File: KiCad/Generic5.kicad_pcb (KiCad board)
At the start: 2 copper layers, 12.5 x 31 mm, 28 parts, among them J1 Conn_01x04, J2 USB-C, U1 ESP32-PICO-MINI-02, U2 FT231XQ, U3 LMR16006+FB

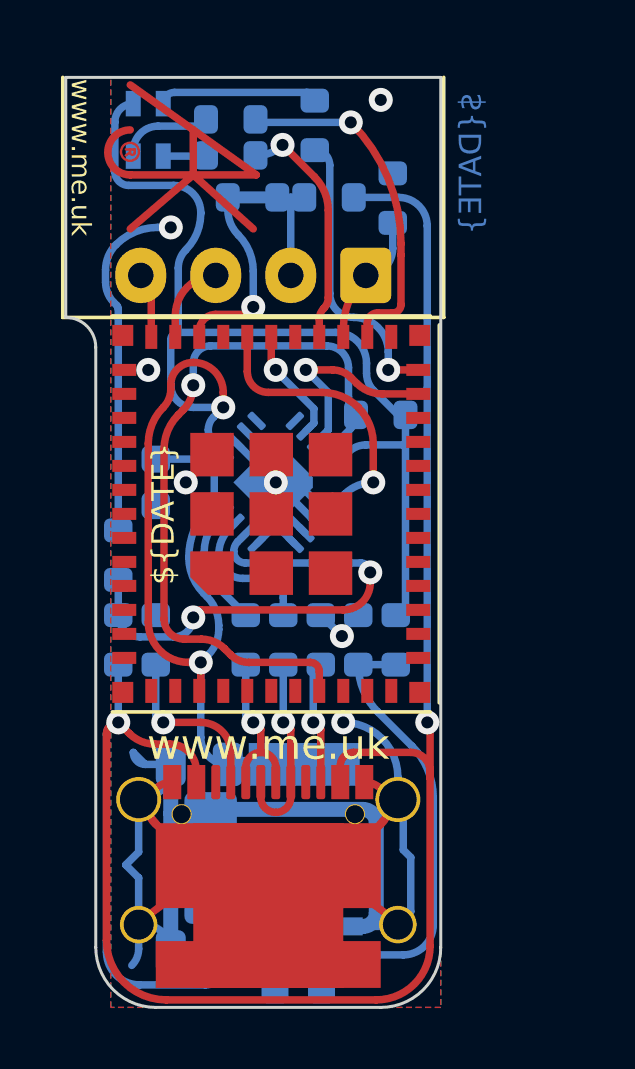
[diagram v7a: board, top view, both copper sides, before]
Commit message: Added buzzer
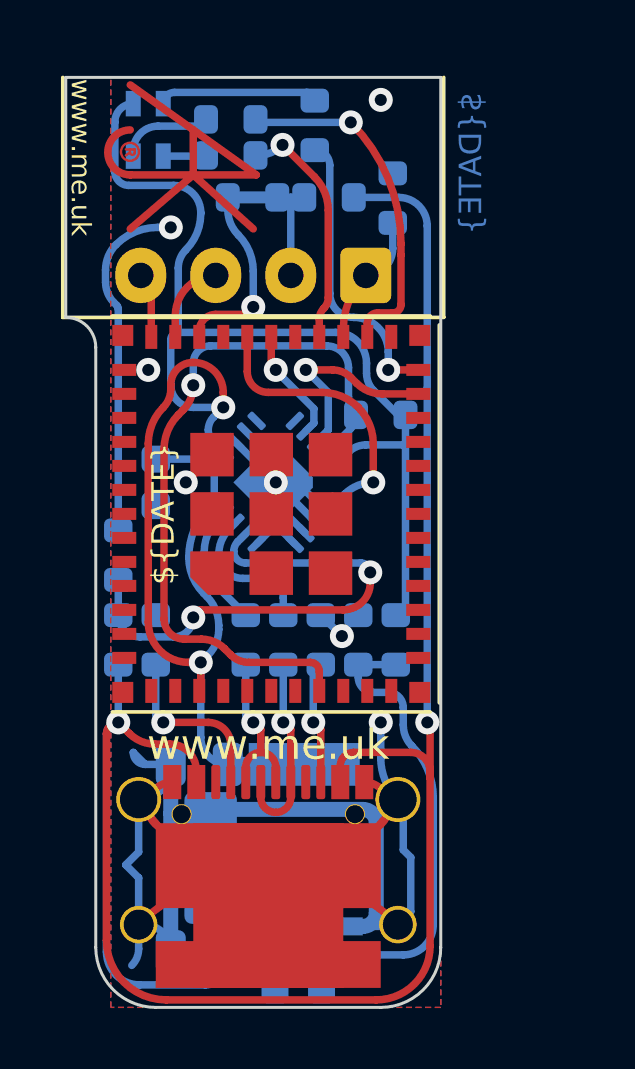
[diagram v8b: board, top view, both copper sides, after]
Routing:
- net GND: track 46.6 -> 45.7 mm
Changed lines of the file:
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@@
   (segment (start 152.375 33.625) (end 151.5 34.5) (width 0.25) (layer "F.Cu") (net 1))
   (via (at 150.25 30.75) (size 0.8) (drill 0.4) (layers "F.Cu" "B.Cu") (free) (net 1))
-  (via (at 156.75 42.5) (size 0.8) (drill 0.4) (layers "F.Cu" "B.Cu") (free) (net 1))
+  (via (at 158 42.5) (size 0.8) (drill 0.4) (layers "F.Cu" "B.Cu") (free) (net 1))
   (via (at 154.5 34.5) (size 0.8) (drill 0.4) (layers "F.Cu" "B.Cu") (net 1))
   (via (at 151 26) (size 0.8) (drill 0.4) (layers "F.Cu" "B.Cu") (free) (net 1))
@@
   (segment (start 158.51 49.3) (end 156.85 49.3) (width 0.25) (layer "B.Cu") (net 1))
   (segment (start 149.93 47.68) (end 149.5 47.25) (width 0.25) (layer "B.Cu") (net 1))
-  (segment (start 158.57 44.32) (end 158.57 45.07) (width 0.25) (layer "B.Cu") (net 1))
   (segment (start 159 47) (end 159 48.81) (width 0.25) (layer "B.Cu") (net 1))
   (segment (start 158.57 45.07) (end 158.75 45.25) (width 0.25) (layer "B.Cu") (net 1))
@@
   (segment (start 158.75 45.25) (end 158.75 46.75) (width 0.25) (layer "B.Cu") (net 1))
   (segment (start 149.5 47.25) (end 149.93 46.82) (width 0.25) (layer "B.Cu") (net 1))
+  (segment (start 158 42.5) (end 158 43.693899) (width 0.25) (layer "B.Cu") (net 1))
   (segment (start 154.375 34.375) (end 154.5 34.5) (width 0.25) (layer "B.Cu") (net 1))
   (segment (start 149.108578 28.508578) (end 149.2 28.6) (width 0.25) (layer "B.Cu") (net 1))
@@
   (arc (start 150.09 49.24) (mid 150.733467 49.506533) (end 151 50.15) (width 0.25) (layer "B.Cu") (net 1))
   (arc (start 151 44) (mid 150.686604 44.756604) (end 149.93 45.07) (width 0.25) (layer "B.Cu") (net 1))
-  (arc (start 156.75 42.5) (mid 158.036934 43.033066) (end 158.57 44.32) (width 0.25) (layer "B.Cu") (net 1))
   (arc (start 149.175 26.575) (mid 148.916317 26.962145) (end 148.82548 27.418815) (width 0.25) (layer "B.Cu") (net 1))
   (arc (start 148.82548 27.825119) (mid 148.899055 28.195004) (end 149.108578 28.508578) (width 0.25) (layer "B.Cu") (net 1))
@@
   (arc (start 149.93 50.044731) (mid 149.870225 50.34524) (end 149.7 50.6) (width 0.25) (layer "B.Cu") (net 1))
   (arc (start 149.175 26.575) (mid 149.811898 26.149438) (end 150.563172 26) (width 0.25) (layer "B.Cu") (net 1))
+  (arc (start 158 43.693899) (mid 158.148138 44.438639) (end 158.57 45.07) (width 0.25) (layer "B.Cu") (net 1))
   (arc (start 158.57 49.24) (mid 158.552426 49.282426) (end 158.51 49.3) (width 0.25) (layer "B.Cu") (net 1))
   (segment (start 156.65 44.49) (end 156.65 43.95) (width 0.25) (layer "F.Cu") (net 2))
@@
   (segment (start 156.788909 34.898097) (end 156.55061 35.136396) (width 0.25) (layer "B.Cu") (net 28))
   (arc (start 157.75 34.5) (mid 157.229861 34.603462) (end 156.788909 34.898097) (width 0.25) (layer "B.Cu") (net 28))
-  (segment (start 157.904074 42.154074) (end 159.042893 43.292893) (width 0.25) (layer "B.Cu") (net 30))
+  (segment (start 157.75 41.5) (end 158.25 41.5) (width 0.25) (layer "B.Cu") (net 30))
+  (segment (start 158.75 42) (end 158.75 42.585787) (width 0.25) (layer "B.Cu") (net 30))
+  (segment (start 157.25 40.575) (end 157.25 41) (width 0.25) (layer "B.Cu") (net 30))
   (segment (start 157.25 40.575) (end 158.5 40.575) (width 0.25) (layer "B.Cu") (net 30))
   (segment (start 158.75 50.25) (end 156.85 50.25) (width 0.25) (layer "B.Cu") (net 30))
   (segment (start 159.75 45) (end 159.75 49.25) (width 0.25) (layer "B.Cu") (net 30))
-  (arc (start 157.25 40.575) (mid 157.419988 41.429589) (end 157.904074 42.154074) (width 0.25) (layer "B.Cu") (net 30))
   (arc (start 159.75 49.25) (mid 159.457107 49.957107) (end 158.75 50.25) (width 0.25) (layer "B.Cu") (net 30))
+  (arc (start 157.25 41) (mid 157.396447 41.353553) (end 157.75 41.5) (width 0.25) (layer "B.Cu") (net 30))
   (arc (start 159.042893 43.292893) (mid 159.566229 44.07612) (end 159.75 45) (width 0.25) (layer "B.Cu") (net 30))
+  (arc (start 158.75 42.585787) (mid 158.826121 42.96847) (end 159.042893 43.292893) (width 0.25) (layer "B.Cu") (net 30))
+  (arc (start 158.25 41.5) (mid 158.603553 41.646447) (end 158.75 42) (width 0.25) (layer "B.Cu") (net 30))
   (segment (start 156.75 38.75) (end 152 38.75) (width 0.25) (layer "F.Cu") (net 35))
   (segment (start 157.649502 37.5) (end 157.649502 37.850498) (width 0.25) (layer "F.Cu") (net 35))
@@
   (arc (start 153.1 36.8) (mid 153.135448 36.62179) (end 153.236396 36.470711) (width 0.25) (layer "B.Cu") (net 35))
   (arc (start 149.97452 39.64952) (mid 149.462207 39.437313) (end 149.25 38.925) (width 0.25) (layer "B.Cu") (net 35))
-  (segment (start 150.75 42.5) (end 152 42.5) (width 0.25) (layer "F.Cu") (net 42))
-  (segment (start 153 43.5) (end 153 44.49) (width 0.25) (layer "F.Cu") (net 42))
+  (segment (start 153 44.49) (end 153 43.25) (width 0.25) (layer "F.Cu") (net 42))
+  (segment (start 152.25 42.5) (end 150.75 42.5) (width 0.25) (layer "F.Cu") (net 42))
   (via (at 150.75 42.5) (size 0.8) (drill 0.4) (layers "F.Cu" "B.Cu") (net 42))
-  (arc (start 152 42.5) (mid 152.707107 42.792893) (end 153 43.5) (width 0.25) (layer "F.Cu") (net 42))
+  (arc (start 153 43.25) (mid 152.78033 42.71967) (end 152.25 42.5) (width 0.25) (layer "F.Cu") (net 42))
   (segment (start 150.5 40.575) (end 150.5 42.25) (width 0.25) (layer "B.Cu") (net 42))
   (arc (start 150.5 42.25) (mid 150.573223 42.426777) (end 150.75 42.5) (width 0.25) (layer "B.Cu") (net 42))
